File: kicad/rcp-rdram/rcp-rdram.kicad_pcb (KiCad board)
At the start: 2 copper layers, 36.8 x 54.6 mm, 29 parts, among them P1 RDRAM-EDGE, U11 RDRAM18-NUS, U11-2 RDRAM18-NUS, U14 RDRAM18-NUS, U14-2 RDRAM18-NUS, U15 MX8330, X2 14.705MHz

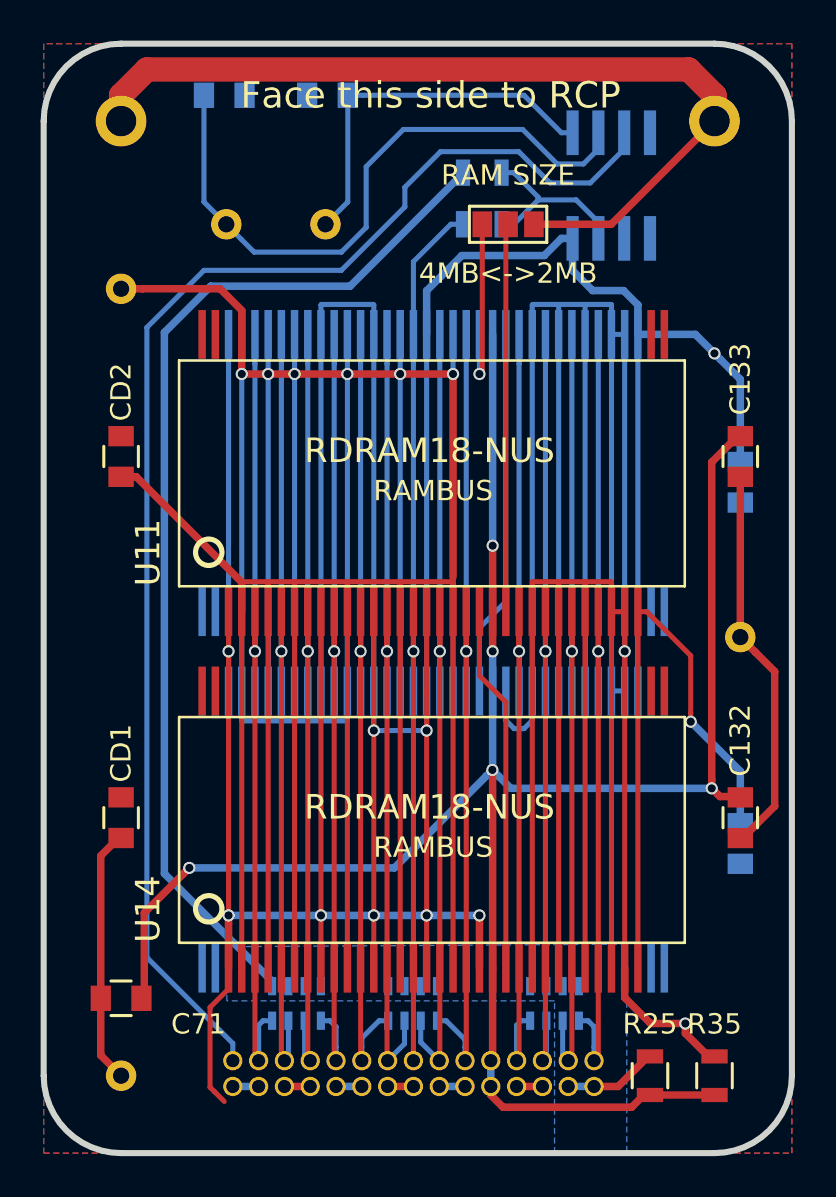
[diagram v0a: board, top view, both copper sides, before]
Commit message: Rerouted top layer with better VDD practice
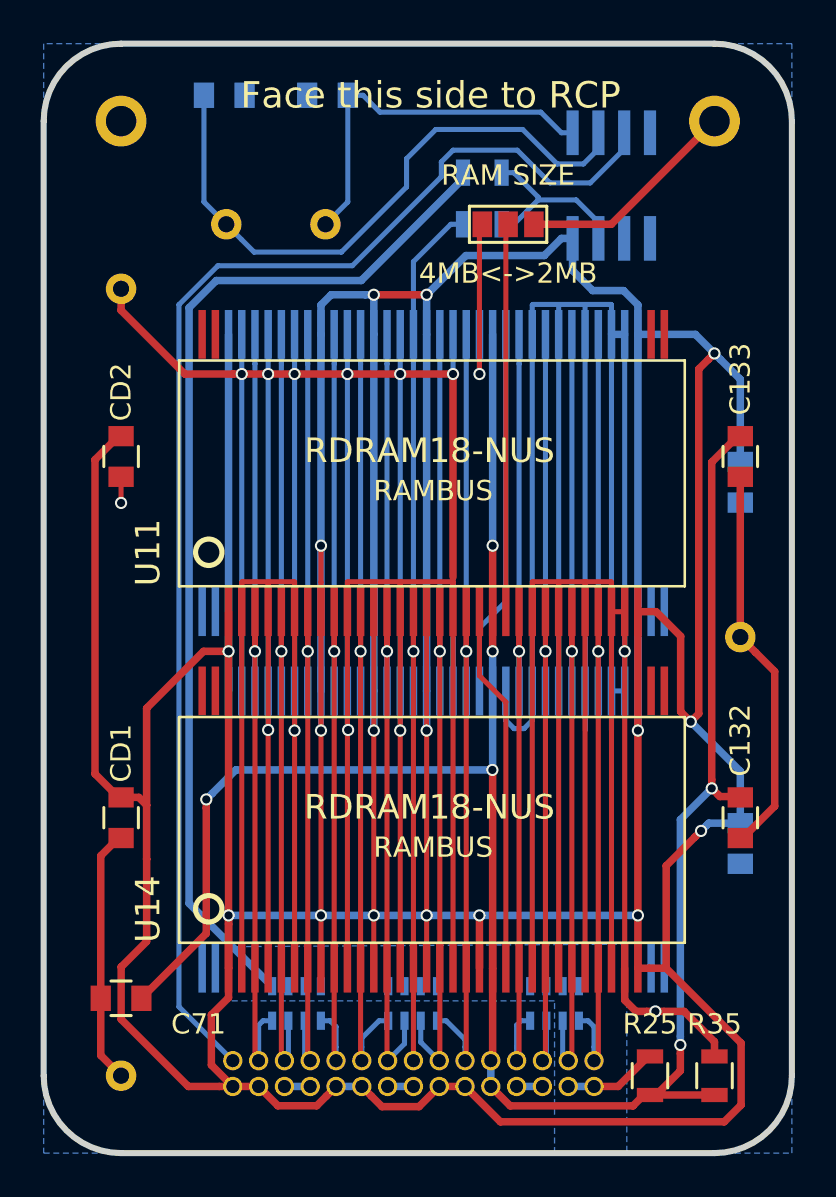
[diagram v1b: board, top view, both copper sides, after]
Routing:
- net VDD: track 258.2 -> 384.4 mm, vias 10 -> 17
- net GND: track 569.7 -> 524.8 mm, vias 8 -> 13
- net /VREF: track 104.1 -> 110.6 mm, vias 5 -> 6
- net Net-(P1-Pad15): track 67.6 -> 66.0 mm
- net Net-(C146-Pad1): track 31.7 -> 30.8 mm
- net /VTERM: track 57.0 -> 56.2 mm
- removed copper zone on F.Cu, net VDD

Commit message: Redo signal termination (a major fail here), power supply lines, going to rewire for 0.1524mm (8mil) line clearance
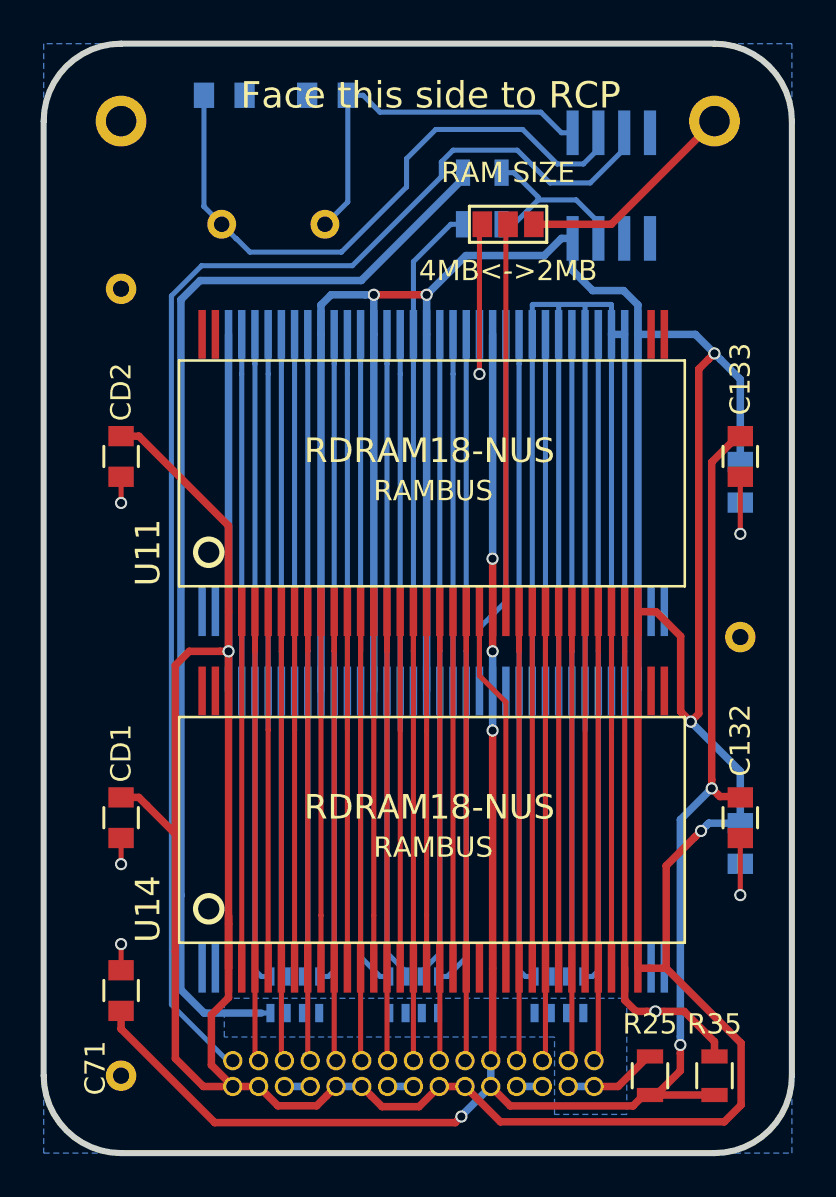
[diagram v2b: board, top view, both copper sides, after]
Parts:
- RA1, RA2, RA3: footprint Resistors_SMD:R_Array_Concave_4x0603 -> n64:cay16-510-j4
- X2: footprint Crystals:Crystal_HC49-U_Vertical -> Crystals:HC-49V
- moved X2 2.41 mm to (115.4, 85.1)
- moved RA3 0.48 mm to (127.0, 123.0)
- moved RA1 0.44 mm to (114.0, 123.0)
- moved RA2 0.44 mm to (119.8, 123.0)
- moved C71 0.38 mm to (105.4, 122.8), turned to 90 degrees
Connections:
- RA1 pad 1: /DQ6 -> /DQ8
- RA1 pad 2: /ADDRESS -> /DQ7
- RA1 pad 3: /DQ7 -> /ADDRESS
- RA1 pad 4: /DQ8 -> /DQ6
- RA2 pad 1: /COMMAND -> /DQ5
- RA2 pad 2: /DQ4 -> /RXCLK
- RA2 pad 3: /RXCLK -> /DQ4
- RA2 pad 4: /DQ5 -> /COMMAND
- RA3 pad 1: /DQ0 -> /DQ3
- RA3 pad 2: /DQ1 -> /DQ2
- RA3 pad 3: /DQ2 -> /DQ1
- RA3 pad 4: /DQ3 -> /DQ0
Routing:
- net GND: track 524.8 -> 440.0 mm, vias 13 -> 6
- net VDD: track 384.4 -> 342.9 mm, vias 17 -> 6
- net /DQ1: track 43.8 -> 56.2 mm, vias 1 -> 0
- net /ADDRESS: track 43.7 -> 56.2 mm, vias 1 -> 0
- net /DQ7: track 43.7 -> 56.1 mm, vias 1 -> 0
- net /DQ2: track 43.7 -> 56.1 mm, vias 1 -> 0
- net /DQ5: track 44.4 -> 56.5 mm, vias 1 -> 0
- net /DQ8: track 44.2 -> 56.3 mm, vias 1 -> 0
- net /DQ3: track 44.2 -> 56.3 mm, vias 1 -> 0
- net /RXCLK: track 43.9 -> 56.0 mm, vias 1 -> 0
- net /COMMAND: track 44.4 -> 56.5 mm, vias 1 -> 0
- net /DQ0: track 44.2 -> 56.3 mm, vias 1 -> 0
- net /DQ6: track 44.2 -> 56.3 mm, vias 1 -> 0
- net /DQ4: track 44.0 -> 56.1 mm, vias 1 -> 0
- net /VREF: track 110.6 -> 106.6 mm
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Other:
- net class Default: clearance 0.15 -> 0.1524
- net class Power removed
- rule trace_clearance: 0.15 -> 0.1524

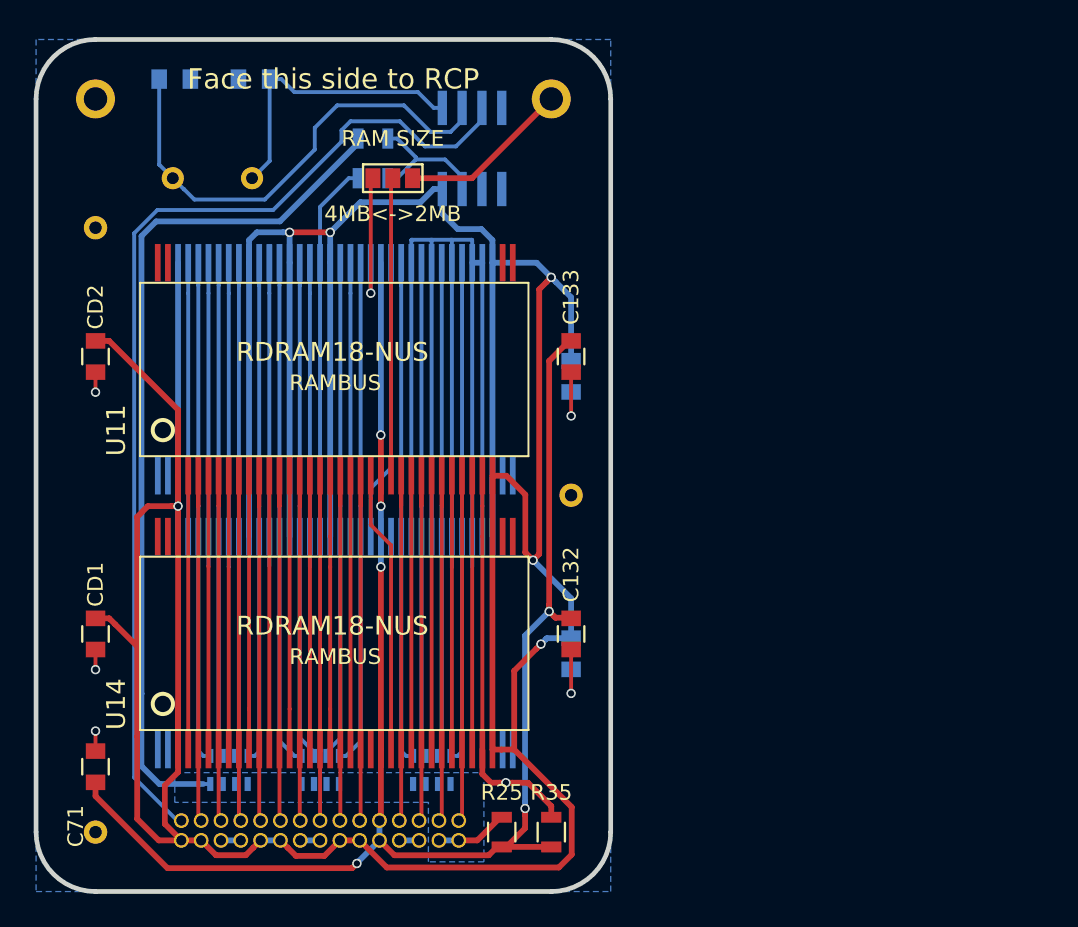
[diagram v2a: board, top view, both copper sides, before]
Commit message: Board changed to L-shape, moved top side RDRAM chips to trick difficult to connect SOUT pin, rewired VREF resistor devider, other improvements
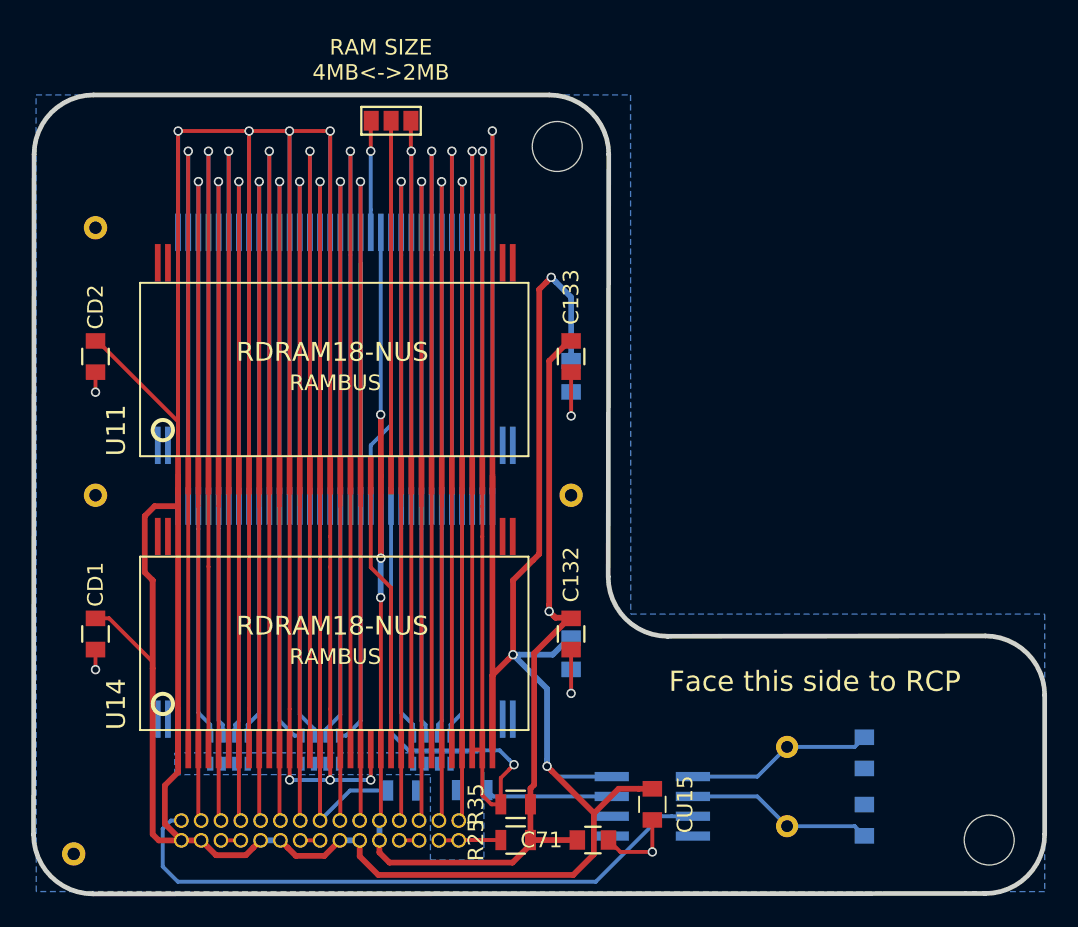
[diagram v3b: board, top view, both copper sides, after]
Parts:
- removed the REF** at (134.6, 80.0)
- removed the REF** at (105.4, 80.0)
- added CU15: 10uF, Capacitors_SMD:C_0805, F.Cu at (141.1, 125.2)
- added REF**: MountingHole_3.2mm_M3, Mounting_Holes:MountingHole_3.2mm_M3, F.Cu at (135.0, 83.1)
- added REF**: MountingHole_2.2mm_M2_DIN965_Pad, Mounting_Holes:MountingHole_2.2mm_M2_DIN965_Pad, F.Cu at (105.4, 105.4)
- added REF**: MountingHole_3.2mm_M3, Mounting_Holes:MountingHole_3.2mm_M3, F.Cu at (162.7, 127.5)
- moved C146 64.9 mm to (154.7, 126.2), turned to 90 degrees
- moved C147 58.3 mm to (154.7, 121.9), turned to 270 degrees
- moved X2 50.0 mm to (149.7, 121.5), turned to 270 degrees
- moved U15 43.7 mm to (141.1, 125.3), turned to 90 degrees
- moved R32 42.2 mm to (129.6, 124.3)
- moved R33 39.3 mm to (125.1, 124.3)
- moved C71 32.2 mm to (137.3, 127.5), turned to 0 degrees
- moved JP1 3.68 mm to (124.3, 81.4)
- moved R35 2.90 mm to (132.3, 125.2), turned to 180 degrees
- moved REF** 1.98 mm to (104.0, 128.4)
- moved U14-2 1.95 mm to (120.8, 94.5)
- moved U11-2 1.95 mm to (120.8, 112.1)
- moved RA1 1.30 mm to (114.0, 121.7)
- moved RA2 1.30 mm to (119.8, 121.7)
- moved RA3 1.30 mm to (127.0, 121.7)
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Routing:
- net GND: track 440.0 -> 726.8 mm, vias 6 -> 17
- net VDD: track 342.9 -> 488.5 mm, vias 6 -> 11
- net /VTERM: track 60.1 -> 3.97 mm
- net /COMMAND: track 56.5 -> 94.9 mm, vias 0 -> 1
- net Net-(P1-Pad15): track 66.9 -> 40.2 mm
- net /DQ7: track 56.1 -> 78.9 mm, vias 0 -> 1
- net /DQ5: track 56.5 -> 79.3 mm, vias 0 -> 1
- net /RXCLK: track 56.0 -> 78.8 mm, vias 0 -> 1
- net /DQ4: track 56.1 -> 78.8 mm, vias 0 -> 1
- net /DQ8: track 56.3 -> 78.8 mm, vias 0 -> 1
- net /DQ0: track 56.3 -> 78.8 mm, vias 0 -> 1
- net /DQ3: track 56.3 -> 78.8 mm, vias 0 -> 1
- net /DQ6: track 56.3 -> 78.8 mm, vias 0 -> 1
- net /DQ2: track 56.1 -> 78.6 mm, vias 0 -> 1
- net /DQ1: track 56.2 -> 78.6 mm, vias 0 -> 1
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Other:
- board size 36.8 x 54.6 mm -> 64.8 x 51.2 mm
- net class Default: clearance 0.1524 -> 0.2
- rule trace_clearance: 0.1524 -> 0.2

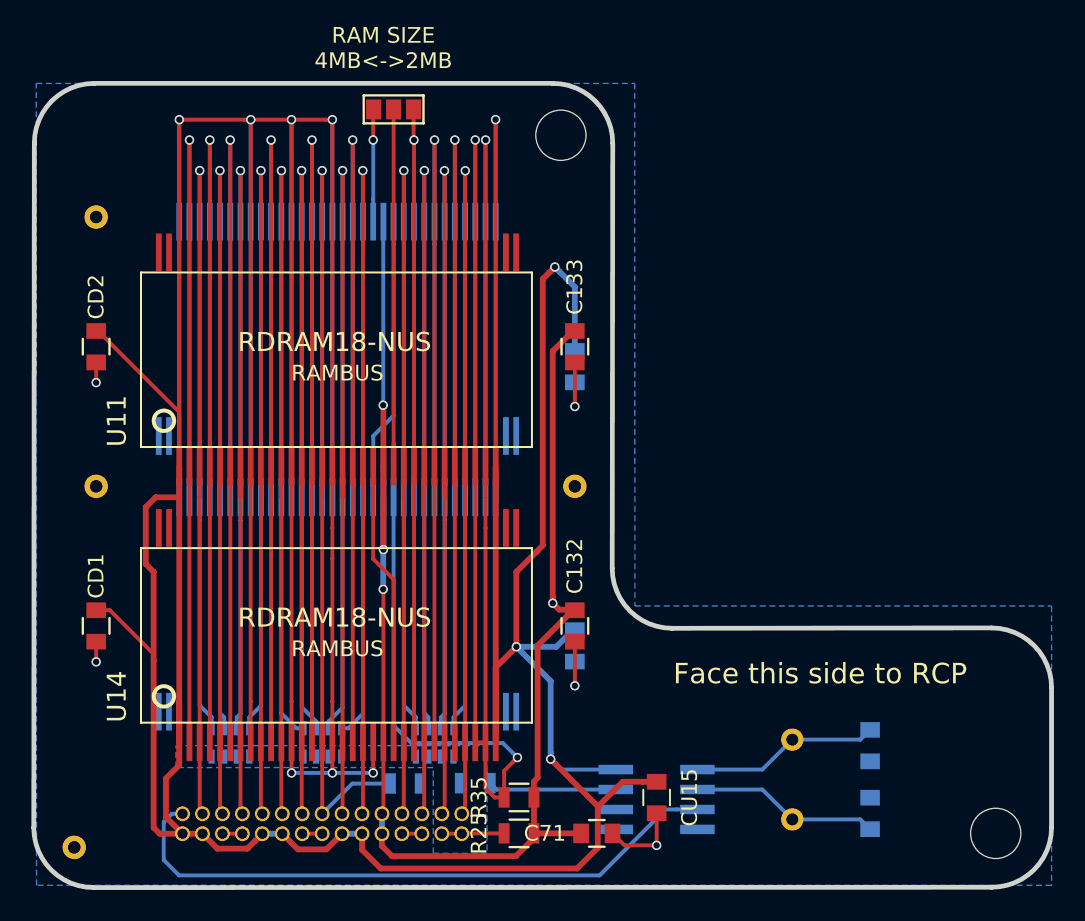
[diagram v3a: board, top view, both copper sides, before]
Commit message: Dimensions added, capacitors moved around, getting ready to shrink the board
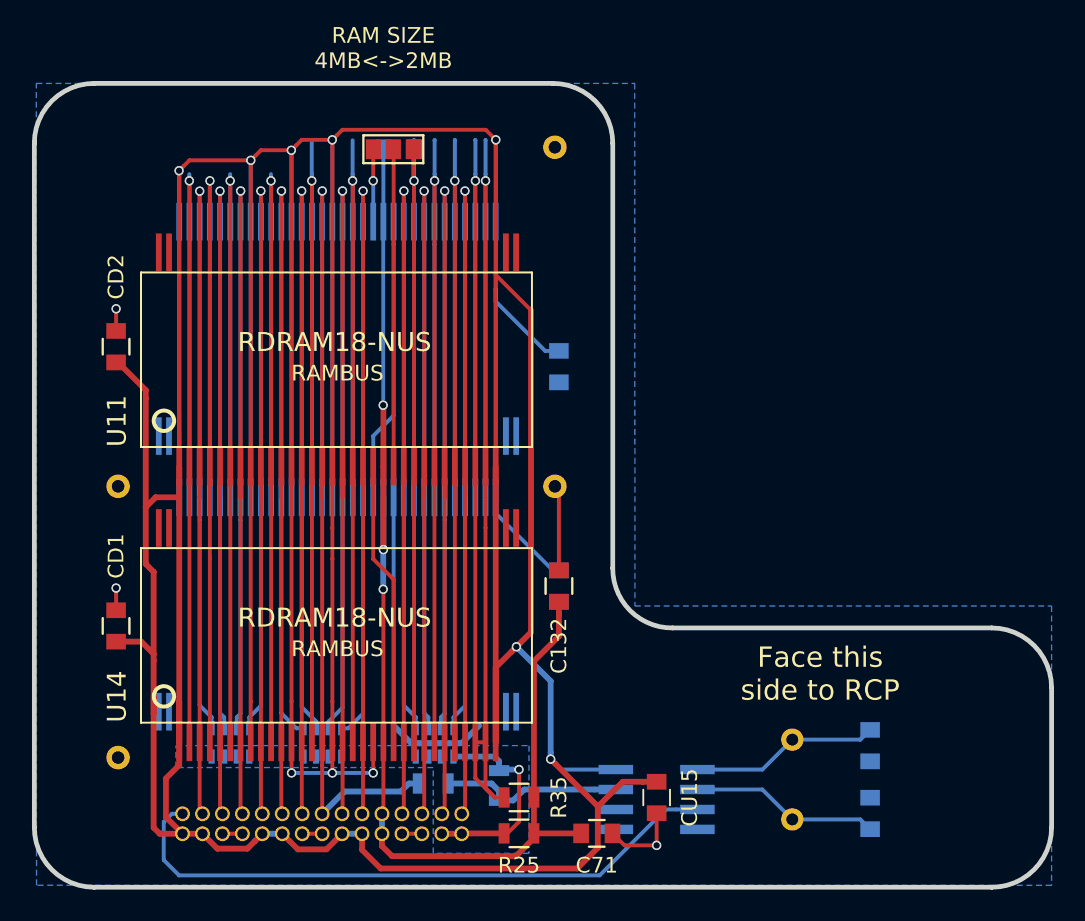
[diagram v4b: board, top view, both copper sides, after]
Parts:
- removed the REF** at (135.0, 83.1)
- removed the REF** at (162.7, 127.5)
- C133: moved to B.Cu
- moved REF** 29.5 mm to (134.6, 83.8)
- moved C133 16.8 mm to (124.7, 83.9), turned to 0 degrees
- moved REF** 6.36 mm to (106.8, 122.7)
- moved CD4 3.94 mm to (134.9, 111.8)
- moved C132 2.74 mm to (134.9, 111.8), turned to 90 degrees
- moved JP1 2.54 mm to (124.3, 83.9)
- moved R33 1.78 mm to (126.9, 124.3)
- moved R32 1.52 mm to (131.1, 124.5), turned to 90 degrees
- moved REF** 1.40 mm to (106.8, 105.4)
- moved CD1 1.27 mm to (106.7, 114.3), turned to 90 degrees
- moved CD2 1.27 mm to (106.7, 96.5), turned to 90 degrees
- moved REF** 1.27 mm to (134.6, 105.4)
- moved CD3 1.02 mm to (134.9, 97.8)
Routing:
- net GND: track 726.8 -> 688.0 mm, vias 17 -> 14
- net /VREF: track 91.8 -> 76.9 mm, vias 4 -> 3
- net /VTERM: track 3.97 -> 13.5 mm, vias 0 -> 1
- net VDD: track 488.5 -> 484.4 mm, vias 11 -> 10
- net Net-(JP1-Pad2): track 24.2 -> 20.2 mm
- net Net-(R32-Pad1): track 8.16 -> 11.8 mm
- net /DQ7: track 78.9 -> 76.3 mm
- net /DQ8: track 78.8 -> 76.2 mm
- net /COMMAND: track 94.9 -> 92.3 mm
- net /RXCLK: track 78.8 -> 76.2 mm
- net /DQ5: track 79.3 -> 76.7 mm
- net /DQ2: track 78.6 -> 76.0 mm
- net /DQ1: track 78.6 -> 76.0 mm
- net /DQ4: track 78.8 -> 76.2 mm
- net /DQ0: track 78.8 -> 76.2 mm
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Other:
- outline, holes or cut-outs redrawn
- board text added: "N64 RAM board v.2"
- board text removed: "N64 RAM board v1.3"

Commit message: Revision 2, mostly finished, TODO: checks
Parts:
- added REF**: MountingHole_2.2mm_M2_DIN965_Pad, Mounting_Holes:MountingHole_2.2mm_M2_DIN965_Pad, F.Cu at (67.4, 64.8)
- added REF**: MountingHole_2.2mm_M2_DIN965_Pad, Mounting_Holes:MountingHole_2.2mm_M2_DIN965_Pad, F.Cu at (67.4, 53.3)
- added REF**: MountingHole_2.2mm_M2_DIN965_Pad, Mounting_Holes:MountingHole_2.2mm_M2_DIN965_Pad, F.Cu at (25.5, 20.3)
- moved C146 110.6 mm to (63.6, 63.5), turned to 270 degrees
- moved X2 110.5 mm to (61.1, 55.5), turned to 180 degrees
- moved C147 110.3 mm to (63.6, 59.7), turned to 90 degrees
- moved U15 105.1 mm to (57.4, 61.8)
- moved REF** 103.1 mm to (25.5, 41.9)
- moved C71 103.0 mm to (56.1, 64.0)
- moved CD1 103.0 mm to (25.5, 50.8)
- moved R25 103.0 mm to (51.2, 64.0)
- moved R33 103.0 mm to (45.7, 60.8)
- moved REF** 103.0 mm to (53.5, 41.9)
- moved U11 103.0 mm to (39.6, 34.7)
- moved U11-2 103.0 mm to (39.6, 48.6)
- moved U14 103.0 mm to (39.6, 52.3)
- moved C132 103.0 mm to (53.7, 48.3)
- moved C133 103.0 mm to (43.6, 20.4)
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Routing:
- net VDD: track 484.4 -> 514.8 mm, vias 10 -> 11
- net GND: track 688.0 -> 672.5 mm
- net Net-(C147-Pad1): track 12.0 -> 8.83 mm
- net Net-(R32-Pad1): track 11.8 -> 9.22 mm
- net Net-(P1-Pad15): track 40.2 -> 37.7 mm
- net /VTERM: track 13.5 -> 12.9 mm
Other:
- board size 64.8 x 51.2 mm -> 47.1 x 49.7 mm
- board text added: "4MB<->2MB"
- board text removed: "RAM SIZE 4MB<->2MB"
